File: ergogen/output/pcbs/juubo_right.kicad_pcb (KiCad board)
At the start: 2 copper layers, 145.5 x 125.5 mm, 45 parts

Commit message: Add right side
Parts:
- added DISP1: RES_ERJ2RKF4701X, RES_ERJ2RKF4701X, F.Cu at (276.2, 84.5)
- added DISP2: RES_ERJ2RKF4701X, RES_ERJ2RKF4701X, F.Cu at (278.1, 84.5)
- added JST1: , JST_PH_S2B-PH-K_02x2.00mm_Angled, F.Cu at (286.5, 91.1)
- added T1: , E73:SPDT_C128955, F.Cu at (286.5, 50.4)
- added _6: , MountingHole_2.2mm_M2_Pad_Via, F.Cu at (319.1, 85.5)
- moved D1 285.8 mm to (385.8, 105.0)
- moved D2 285.8 mm to (385.8, 86.0)
- moved D3 285.8 mm to (385.8, 66.9)
- moved S1 285.8 mm to (385.8, 100.0)
- moved S2 285.8 mm to (385.8, 81.0)
- moved S3 285.8 mm to (385.8, 61.9)
- moved _3 267.4 mm to (376.2, 86.7)
- moved _1 266.7 mm to (376.2, 67.6)
- moved D4 247.6 mm to (366.7, 100.0)
- moved D5 247.6 mm to (366.7, 81.0)
- moved D6 247.6 mm to (366.7, 61.9)
- moved S4 247.6 mm to (366.7, 95.0)
- moved S5 247.6 mm to (366.7, 76.0)
- moved S6 247.6 mm to (366.7, 56.9)
- moved D7 209.5 mm to (347.6, 97.5)
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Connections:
- net extra_cluster renamed mirror_extra_cluster
- net index_bottom renamed mirror_index_bottom
- net index_home renamed mirror_index_home
- net index_top renamed mirror_index_top
- net inner_bottom renamed mirror_inner_bottom
- net inner_home renamed mirror_inner_home
- net inner_top renamed mirror_inner_top
- net layer_cluster renamed mirror_layer_cluster
- net middle_bottom renamed mirror_middle_bottom
- net middle_home renamed mirror_middle_home
- net middle_top renamed mirror_middle_top
- net pinky_bottom renamed mirror_pinky_bottom
- net pinky_home renamed mirror_pinky_home
- net pinky_top renamed mirror_pinky_top
- net ring_bottom renamed mirror_ring_bottom
- net ring_home renamed mirror_ring_home
- net ring_top renamed mirror_ring_top
- net space_cluster renamed mirror_space_cluster
- ROT1 pad 1: P9 -> P19
- ROT1 pad A: P7 -> P20
- ROT1 pad B: P8 -> P21
- S1 pad 1: P18 -> P4
- S10 pad 1: P21 -> P7
- S11 pad 1: P21 -> P7
- S12 pad 1: P21 -> P7
- S13 pad 1: P1 -> P8
- S14 pad 1: P1 -> P8
- S15 pad 1: P1 -> P8
- S16 pad 1: P20 -> P6
- S17 pad 1: P21 -> P7
- S18 pad 1: P1 -> P8
- S2 pad 1: P18 -> P4
- S3 pad 1: P18 -> P4
- S4 pad 1: P19 -> P5
- S5 pad 1: P19 -> P5
- S6 pad 1: P19 -> P5
- S7 pad 1: P20 -> P6
- S8 pad 1: P20 -> P6
- S9 pad 1: P20 -> P6
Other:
- board size 145.5 x 125.5 mm -> 145.6 x 125.5 mm

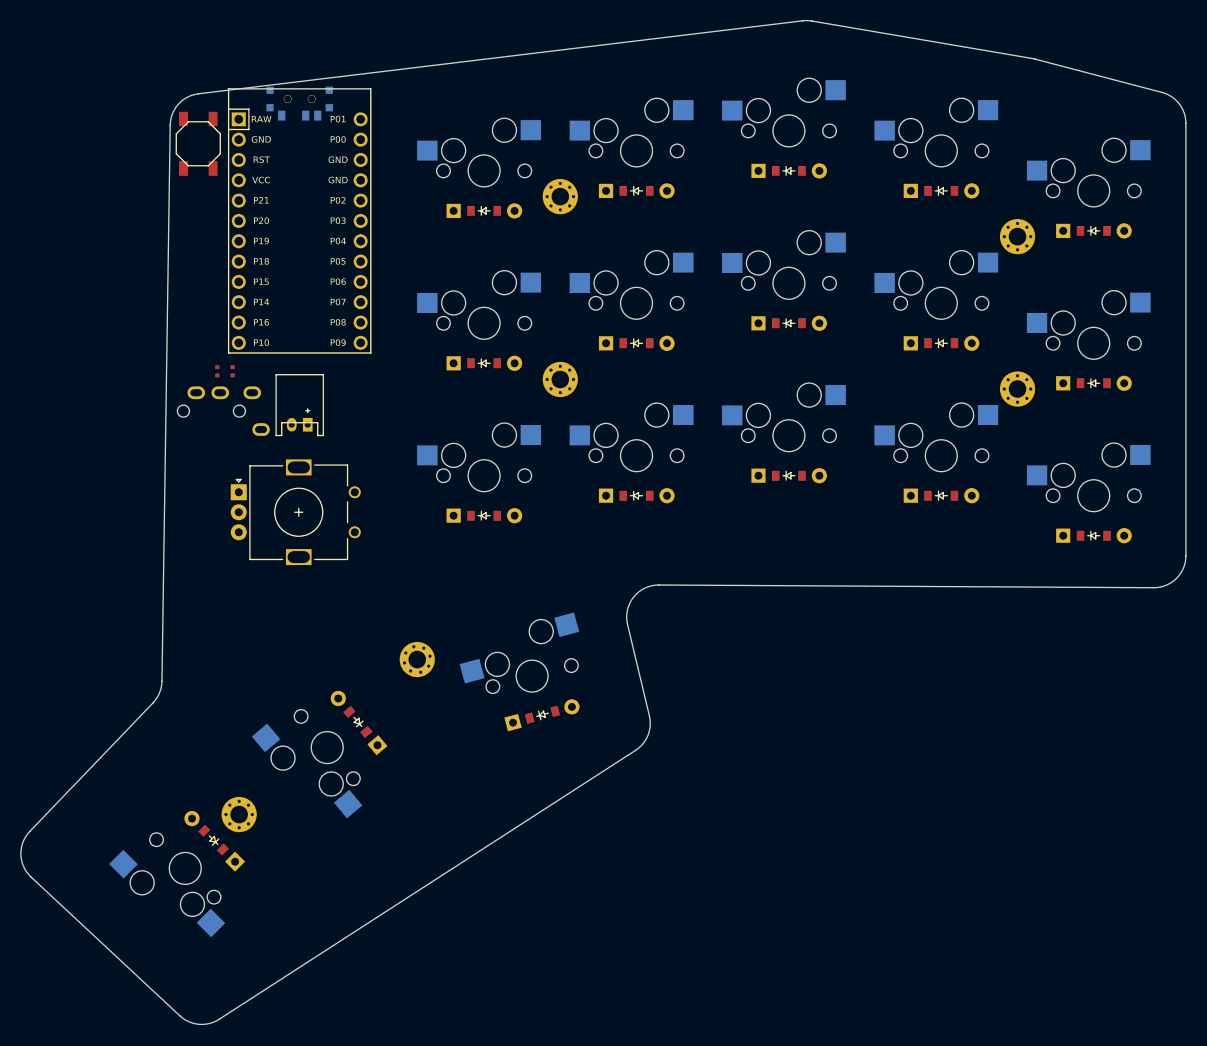
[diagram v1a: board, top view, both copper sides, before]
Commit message: Heighten case wall & plate thickness, left side
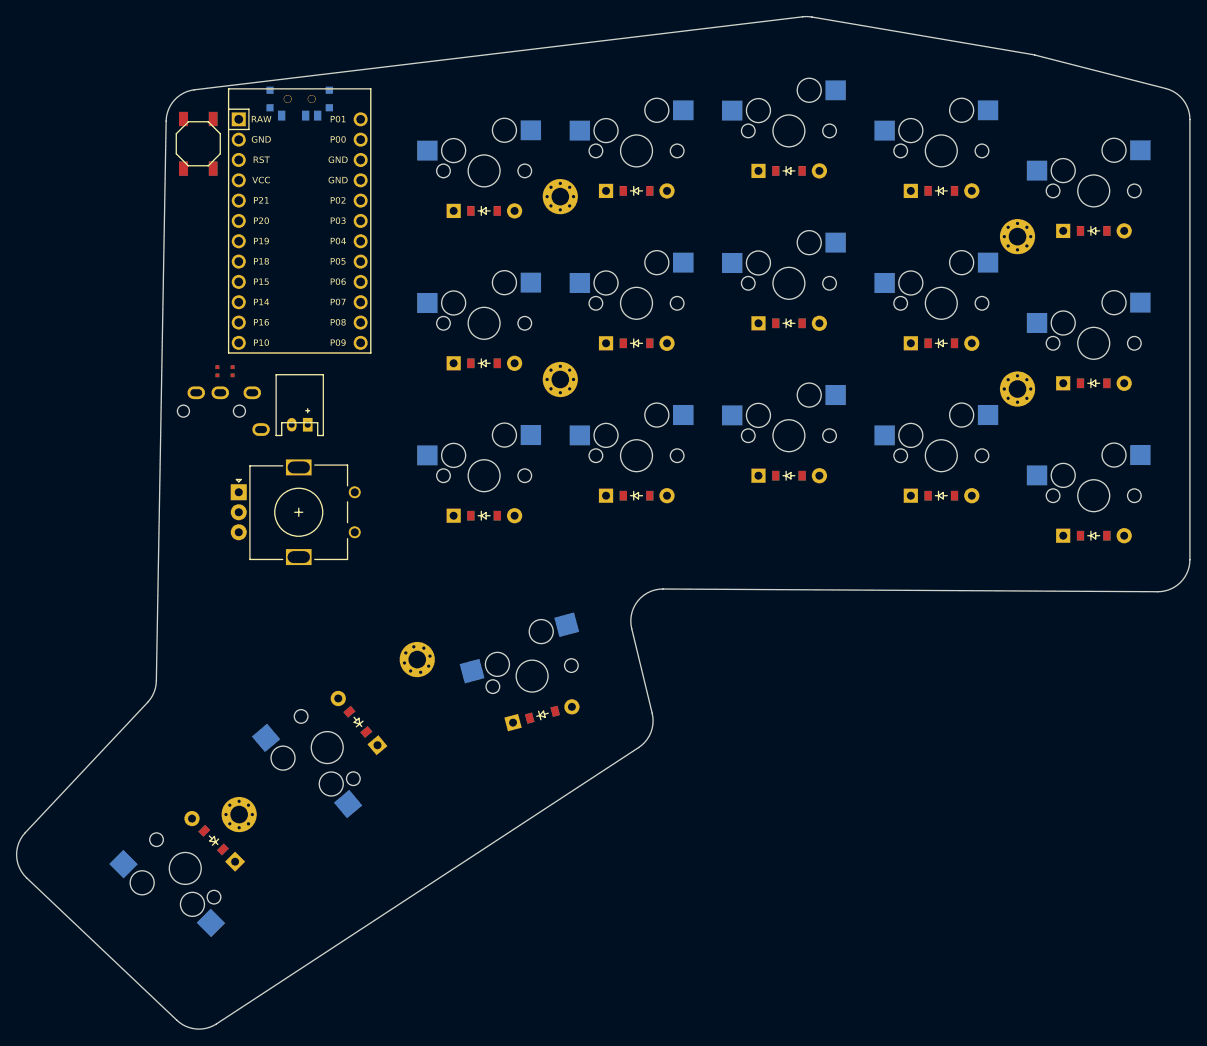
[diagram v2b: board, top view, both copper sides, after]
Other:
- board size 145.6 x 125.5 mm -> 146.7 x 126.6 mm
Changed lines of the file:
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@@
       (pad "1" thru_hole circle locked (at 0 -1.65) (size 0.7 0.7) (drill 0.4) (layers *.Cu *.Mask))
     )
-            (gr_line (start 397.275 107.50296162142857) (end 397.275 53.46061479002625) (angle 90) (layer Edge.Cuts) (width 0.15))
-(gr_line (start 394.29047356377947 49.59165972802612) (end 378.3959609577913 45.41987164246493) (angle 90) (layer Edge.Cuts) (width 0.15))
-(gr_line (start 378.05074741053147 45.345382607272875) (end 350.52786362543645 40.66736857871321) (angle 90) (layer Edge.Cuts) (width 0.15))
-(gr_line (start 349.3781107998899 40.639655801144094) (end 273.833207725321 49.76123537830966) (angle 90) (layer Edge.Cuts) (width 0.15))
-(gr_line (start 270.31314133731644 53.67301305311412) (end 269.2810380690971 123.19177812521593) (angle 90) (layer Edge.Cuts) (width 0.15))
-(gr_line (start 268.1685596178332 125.90093007325783) (end 252.7570680234687 141.97234609192532) (angle 90) (layer Edge.Cuts) (width 0.15))
-(gr_line (start 252.9164303261063 147.66654848617594) (end 271.52717554849835 165.0180803598033) (angle 90) (layer Edge.Cuts) (width 0.15))
-(gr_line (start 276.42492344161667 165.4526132812615) (end 328.49228888486397 131.8273611550129) (angle 90) (layer Edge.Cuts) (width 0.15))
-(gr_line (start 330.2128222574696 127.53789858189953) (end 327.47902444208063 116.09220110959859) (angle 90) (layer Edge.Cuts) (width 0.15))
-(gr_line (start 331.3915648646794 111.16300310365209) (end 393.253022399997 111.50290122197802) (angle 90) (layer Edge.Cuts) (width 0.15))
-(gr_arc (start 393.275 53.46061479002625) (end 397.275 53.46061479002625) (angle -75.293457569409) (layer Edge.Cuts) (width 0.15))
-(gr_arc (start 377.3804873940118 49.28882670446506) (end 378.39596099401183 45.41987160446506) (angle -5.060269060891017) (layer Edge.Cuts) (width 0.15))
-(gr_arc (start 349.85760360891675 44.610812675905386) (end 350.52786360891673 40.667368575905385) (angle -16.531058090283395) (layer Edge.Cuts) (width 0.15))
-(gr_arc (start 274.31270053434787 53.73239225307096) (end 273.83320773434787 49.76123545307096) (angle -82.26463964137555) (layer Edge.Cuts) (width 0.15))
-(gr_arc (start 265.2814788720657 123.13239892526326) (end 268.16855967206567 125.90093012526326) (angle -42.94859990838398) (layer Edge.Cuts) (width 0.15))
-(gr_arc (start 255.64414876923433 144.740877239918) (end 252.75706796923433 141.972346039918) (angle -90.80456151683109) (layer Edge.Cuts) (width 0.15))
-(gr_arc (start 274.2548939916264 162.09240911354533) (end 271.52717559162636 165.01808031354534) (angle -75.8491037335715) (layer Edge.Cuts) (width 0.15))
-(gr_arc (start 326.3222594348737 128.46715698729676) (end 328.49228893487367 131.82736118729676) (angle -70.57889058731709) (layer Edge.Cuts) (width 0.15))
-(gr_arc (start 331.3695872646765 115.16294270420167) (end 331.3915648646765 111.16300310420166) (angle -103.74818780802899) (layer Edge.Cuts) (width 0.15))
-(gr_arc (start 393.275 107.50296162142857) (end 393.25302239999996 111.50290122142857) (angle -90.31480751667874) (layer Edge.Cuts) (width 0.15))
+            (gr_line (start 397.775 108.00296162142858) (end 397.775 52.98073082915601) (angle 90) (layer Edge.Cuts) (width 0.15))
+(gr_line (start 394.76611684187117 49.1054646654402) (end 378.38402872698833 44.915672308692685) (angle 90) (layer Edge.Cuts) (width 0.15))
+(gr_line (start 378.0631719016369 44.847494375216336) (end 350.52636745824896 40.16711427792311) (angle 90) (layer Edge.Cuts) (width 0.15))
+(gr_line (start 349.3795658388905 40.13904635145789) (end 273.32689331337906 49.264607382425126) (angle 90) (layer Edge.Cuts) (width 0.15))
+(gr_line (start 269.8040462179351 53.166192607861376) (end 268.58024329474523 123.16041708043667) (angle 90) (layer Edge.Cuts) (width 0.15))
+(gr_line (start 267.4967761400817 125.82862862927146) (end 252.19239605566645 142.12669744297847) (angle 90) (layer Edge.Cuts) (width 0.15))
+(gr_line (start 252.3572232938916 147.7685368901803) (end 271.1573853977094 165.58063734338276) (angle 90) (layer Edge.Cuts) (width 0.15))
+(gr_line (start 276.0992869331007 166.0236306890619) (end 328.86350697386536 131.48320920349795) (angle 90) (layer Edge.Cuts) (width 0.15))
+(gr_line (start 330.56048929511957 127.1957211694696) (end 327.9973893815331 116.60382196091155) (angle 90) (layer Edge.Cuts) (width 0.15))
+(gr_line (start 331.9071565327879 111.66308877215819) (end 393.75302239999706 112.00290122197802) (angle 90) (layer Edge.Cuts) (width 0.15))
+(gr_arc (start 393.775 52.98073082915601) (end 397.775 52.98073082915601) (angle -75.6538640737767) (layer Edge.Cuts) (width 0.15))
+(gr_arc (start 377.39291188511726 48.79093847240852) (end 378.38402868511724 44.91567237240852) (angle -4.699862556521637) (layer Edge.Cuts) (width 0.15))
+(gr_arc (start 349.8561074417292 44.11055837511528) (end 350.5263674417292 40.16711427511528) (angle -16.488480181305164) (layer Edge.Cuts) (width 0.15))
+(gr_arc (start 273.8034349162177 53.23611940608251) (end 273.3268933162177 49.26460730608251) (angle -82.15611455141611) (layer Edge.Cuts) (width 0.15))
+(gr_arc (start 264.5808545964626 123.09049028221489) (end 267.4967760964626 125.82862858221489) (angle -42.19733729001075) (layer Edge.Cuts) (width 0.15))
+(gr_arc (start 255.10831759928521 144.86483579003476) (end 252.19239609928522 142.12669749003476) (angle -89.74489033300014) (layer Edge.Cuts) (width 0.15))
+(gr_arc (start 273.9084797031029 162.6769362432372) (end 271.1573854031029 165.5806373432372) (angle -76.66361533542275) (layer Edge.Cuts) (width 0.15))
+(gr_arc (start 326.67269974386755 128.13651475767327) (end 328.86350694386755 131.48320915767326) (angle -70.39382807020672) (layer Edge.Cuts) (width 0.15))
+(gr_arc (start 331.885178932785 115.66302837270769) (end 331.907156532785 111.66308877270768) (angle -103.9181253283114) (layer Edge.Cuts) (width 0.15))
+(gr_arc (start 393.775 108.00296162142858) (end 393.75302239999996 112.00290122142859) (angle -90.31480751667794) (layer Edge.Cuts) (width 0.15))
 )
